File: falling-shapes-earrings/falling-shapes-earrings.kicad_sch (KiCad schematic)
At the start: 28 parts, among them U1 ATTINY85-20SUR

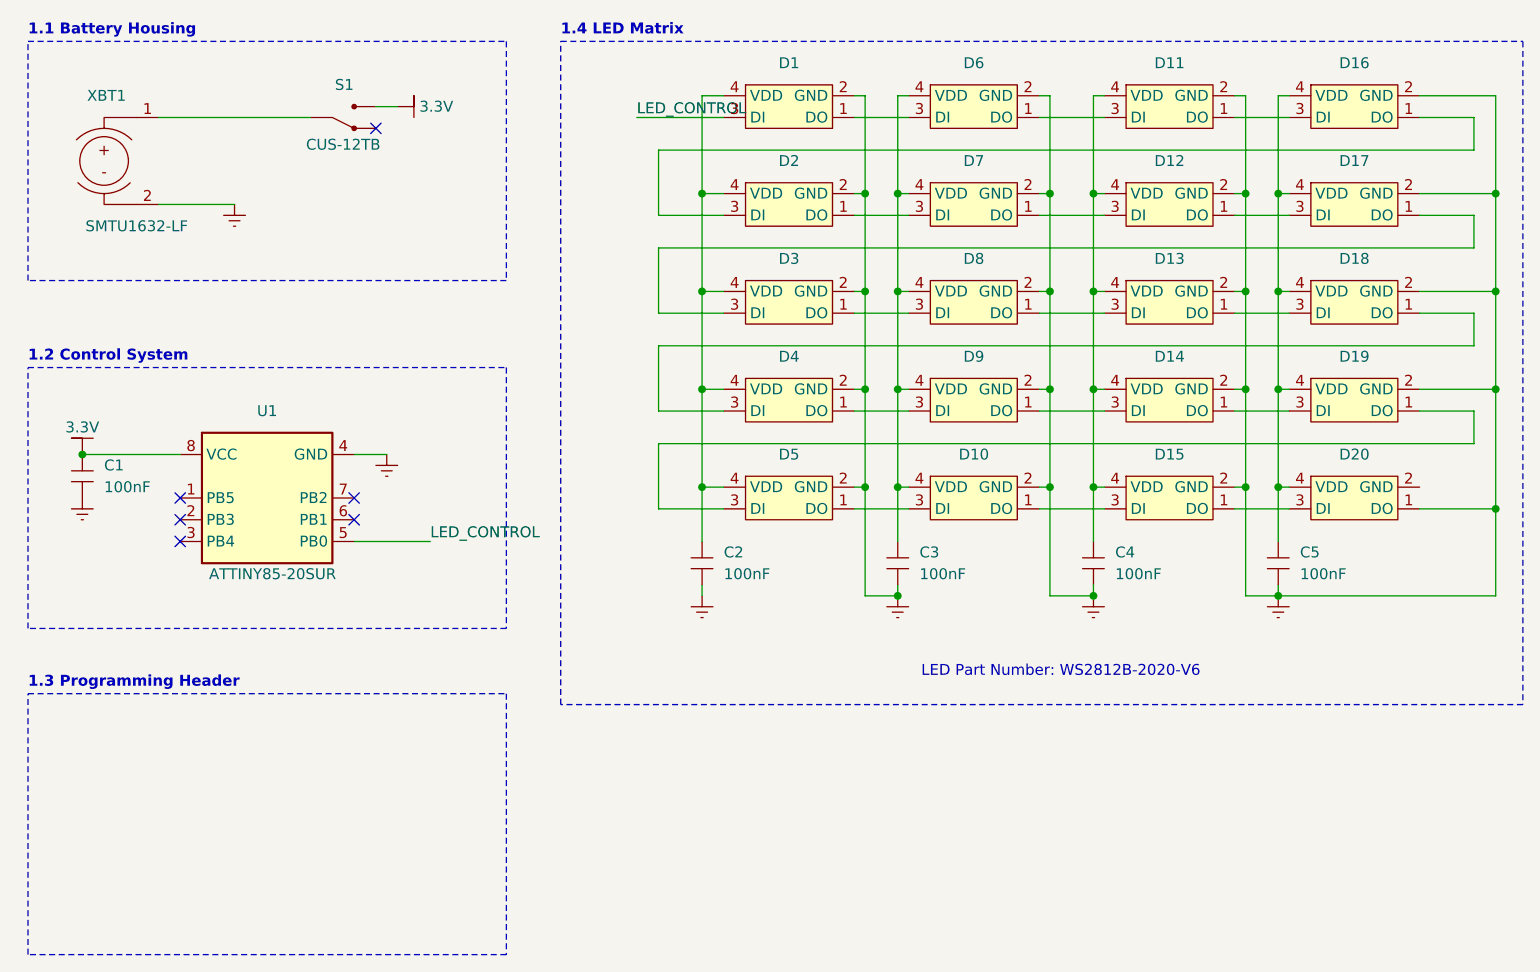
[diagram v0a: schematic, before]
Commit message: Update falling-shapes-earrings.kicad_sch
Ran an ERC and corrected errors
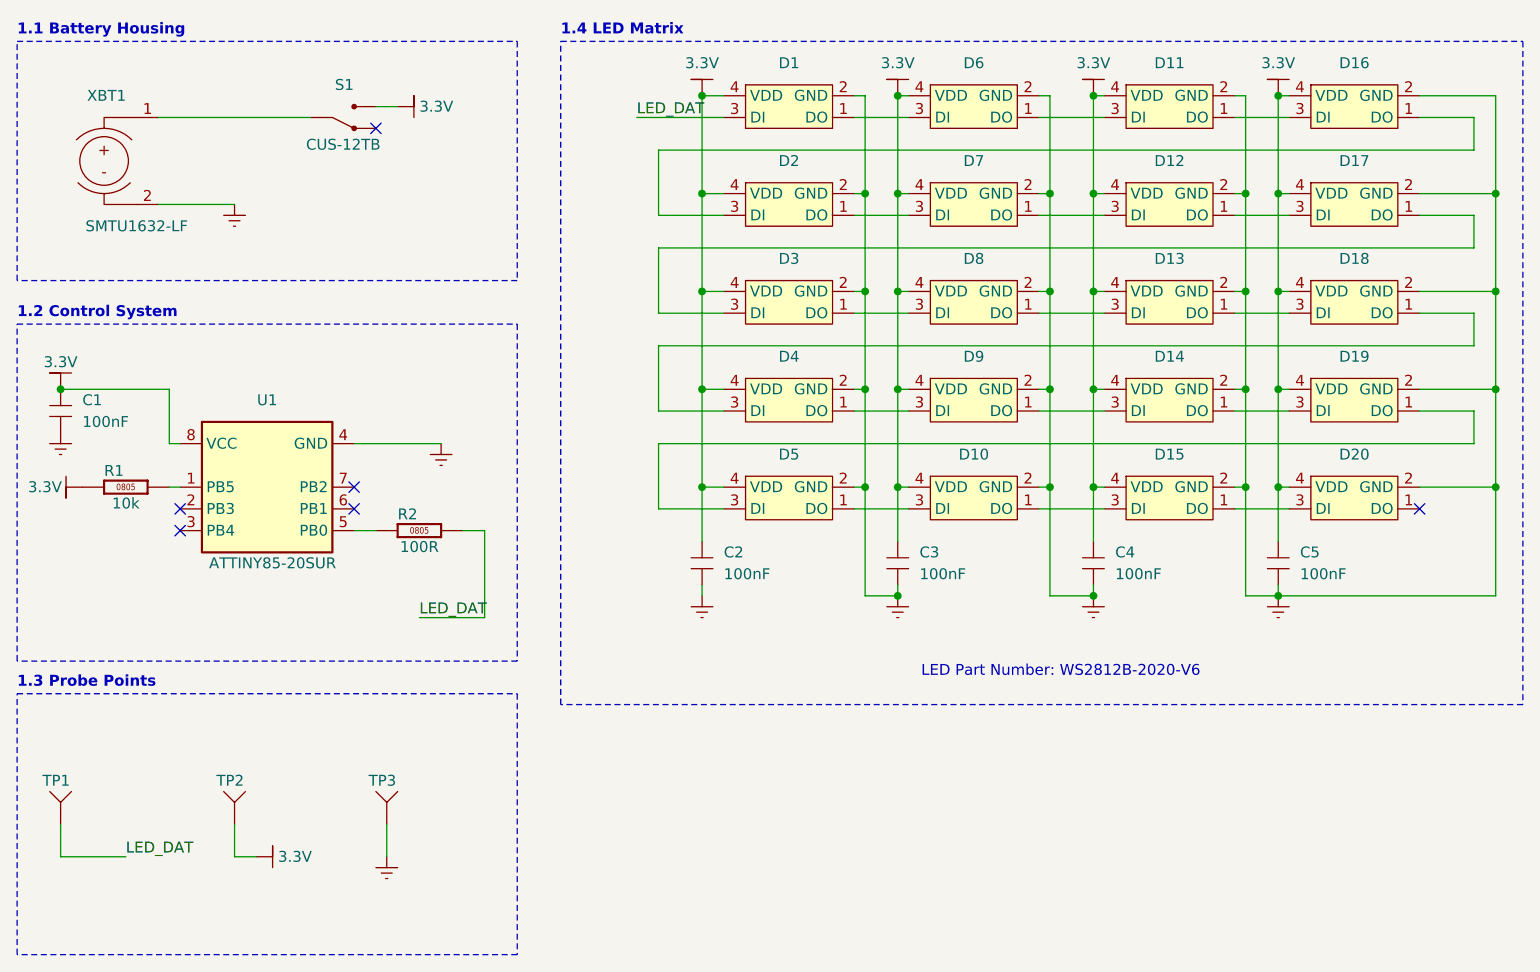
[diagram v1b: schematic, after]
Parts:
- added R1: 10k, Resistors:R0805_0_25, symbol Resistors:RC0805JR-1310KL
- added R2: 100R, Resistors:R0805_0_25, symbol Resistors:RC0805FR-07100RL
- added TP1, TP2, TP3: (no value), Test Points:Test Pad, symbol Test Points:Test Pad
- D1, D10, D11, D12, D13, D14, D15, D16, D17, D18, D19, D2, D20, D3, D4, D5, D6, D7, D8, D9: MSL Not Specified -> 5a (24h)
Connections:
- net 3.3V: now also C2.2, C3.2, C4.2, C5.2, D1.4 (VDD), D10.4 (VDD), D11.4 (VDD), D12.4 (VDD), D13.4 (VDD), D14.4 (VDD), D15.4 (VDD), D16.4 (VDD), D17.4 (VDD), D18.4 (VDD), D19.4 (VDD), D2.4 (VDD), D20.4 (VDD), D3.4 (VDD), D4.4 (VDD), D5.4 (VDD), D6.4 (VDD), D7.4 (VDD), D8.4 (VDD), D9.4 (VDD), R1.1, TP2.1 (Test)
- net GNDREF: now also D20.2 (GND), TP3.1 (Test); no longer D20.1 (DO)
- net at U1.1 (PB5): now also R1.2
- net LED_CONTROL: no longer names the net of U1.5 (PB0)
- net LED_CONTROL: now also R2.1; no longer D1.3 (DI)
- new net LED_DAT: D1.3 (DI), R2.2, TP1.1 (Test)
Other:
- note added: "1.3 Probe Points"
- note removed: "1.3 Programming Header"
- moved on the sheet: C1, U1
